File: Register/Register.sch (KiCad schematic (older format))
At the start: 22 parts, among them J1 Conn_01x16, J2 Conn_01x16, J3 Conn_01x08, J4 Conn_01x08, J5 Conn_01x12, U1 SN74LS04N, U2 74LS173, U3 74LS173, U4 74LS245

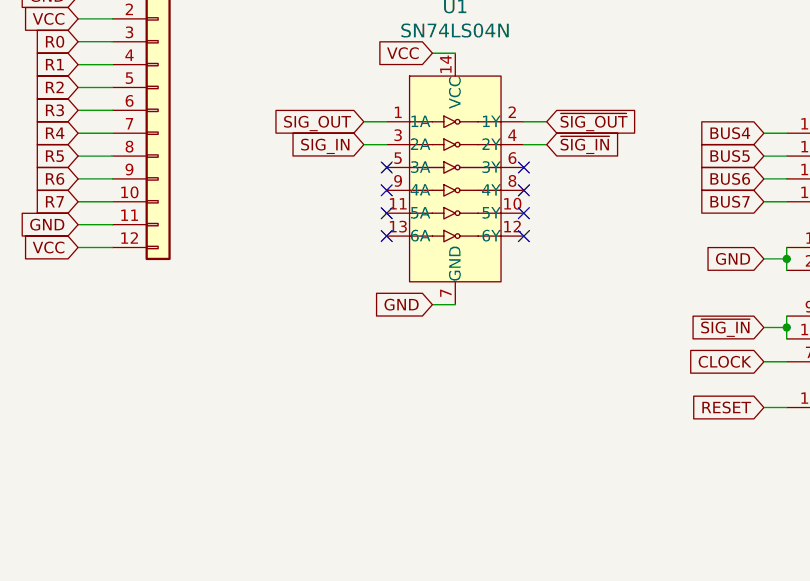
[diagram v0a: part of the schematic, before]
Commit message: Fixed floating inputs; improved power; added parts list; replaced JK latches
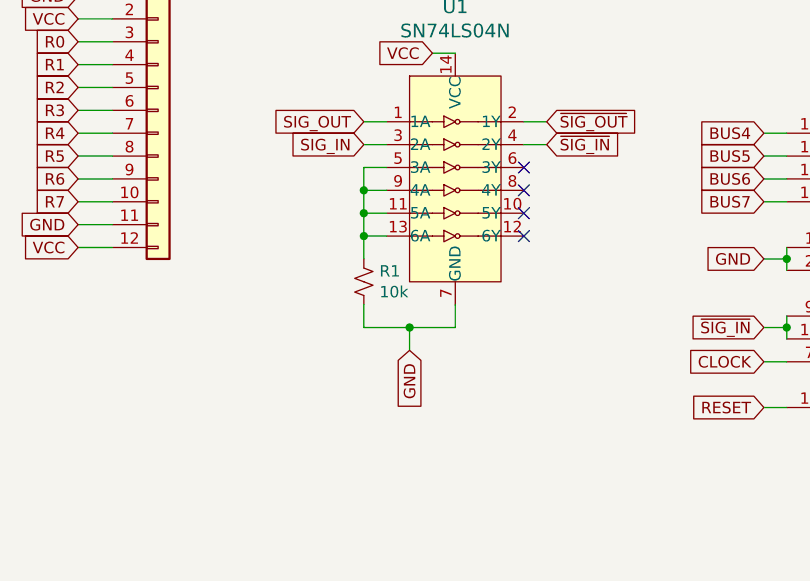
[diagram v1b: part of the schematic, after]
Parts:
- added R1: 10k, Resistor_THT:R_Axial_DIN0207_L6.3mm_D2.5mm_P7.62mm_Horizontal, symbol Device:R_Small_US
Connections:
- net GND: now also R1.1
- net at U1.11 (5A): now also U1.13 (6A), U1.5 (3A), U1.9 (4A), R1.2
- no-connect marks 8 -> 4
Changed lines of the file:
@@
 Wire Wire Line
 	8800 1750 8650 1750
-Text GLabel 4600 4100 0    50   Input ~ 0
-GND
-Wire Wire Line
-	4600 4100 4700 4100
+Text GLabel 4500 4300 3    50   Input ~ 0
+GND
 $Comp
 L Connector_Generic:Conn_01x08 J4
@@
 Wire Wire Line
 	9300 5200 9950 5200
-NoConn ~ 4400 3500
-NoConn ~ 4400 3600
-NoConn ~ 4400 3700
-NoConn ~ 4400 3800
 NoConn ~ 5000 3500
 NoConn ~ 5000 3600
@@
 Wire Wire Line
 	3050 3850 3200 3850
+Wire Wire Line
+	4400 3500 4300 3500
+Wire Wire Line
+	4300 3500 4300 3600
+Wire Wire Line
+	4400 3600 4300 3600
+Connection ~ 4300 3600
+Wire Wire Line
+	4300 3600 4300 3700
+Wire Wire Line
+	4400 3700 4300 3700
+Connection ~ 4300 3700
+Wire Wire Line
+	4300 3700 4300 3800
+Wire Wire Line
+	4400 3800 4300 3800
+$Comp
+L Device:R_Small_US R1
+U 1 1 60473EB3
+P 4300 4000
+F 0 "R1" H 4232 3954 50  0000 R CNN
+F 1 "10k" H 4232 4045 50  0000 R CNN
+F 2 "Resistor_THT:R_Axial_DIN0207_L6.3mm_D2.5mm_P7.62mm_Horizontal" H 4300 4000 50  0001 C CNN
+F 3 "~" H 4300 4000 50  0001 C CNN
+	1    4300 4000
+	-1   0    0    1
+$EndComp
+Wire Wire Line
+	4300 3800 4300 3900
+Connection ~ 4300 3800
+Wire Wire Line
+	4300 4100 4300 4200
+Wire Wire Line
+	4300 4200 4500 4200
+Wire Wire Line
+	4700 4200 4700 4100
+Wire Wire Line
+	4500 4300 4500 4200
+Connection ~ 4500 4200
+Wire Wire Line
+	4500 4200 4700 4200
 $EndSCHEMATC

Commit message: Update all boards to r3, and update revision log and gitignore
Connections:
- net R0: now also D8.2 (A); no longer D1.2 (A)
- net R1: now also D7.2 (A); no longer D2.2 (A)
- net R2: now also D6.2 (A); no longer D3.2 (A)
- net R3: now also D5.2 (A); no longer D4.2 (A)
- net R4: now also D4.2 (A); no longer D5.2 (A)
- net R5: now also D3.2 (A); no longer D6.2 (A)
- net R6: now also D2.2 (A); no longer D7.2 (A)
- net R7: now also D1.2 (A); no longer D8.2 (A)
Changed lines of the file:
@@
 Wire Wire Line
 	4150 900  4150 1050
+Text GLabel 10300 4500 1    50   Input ~ 0
+R0
+Text GLabel 9950 4500 1    50   Input ~ 0
+R1
+Text GLabel 9600 4500 1    50   Input ~ 0
+R2
+Text GLabel 9250 4500 1    50   Input ~ 0
+R3
+Text GLabel 8850 4500 1    50   Input ~ 0
+R4
+Text GLabel 8500 4500 1    50   Input ~ 0
+R5
+Text GLabel 8150 4500 1    50   Input ~ 0
+R6
 Text GLabel 7800 4500 1    50   Input ~ 0
-R0
-Text GLabel 8150 4500 1    50   Input ~ 0
-R1
-Text GLabel 8500 4500 1    50   Input ~ 0
-R2
-Text GLabel 8850 4500 1    50   Input ~ 0
-R3
-Text GLabel 9250 4500 1    50   Input ~ 0
-R4
-Text GLabel 9600 4500 1    50   Input ~ 0
-R5
-Text GLabel 9950 4500 1    50   Input ~ 0
-R6
-Text GLabel 10300 4500 1    50   Input ~ 0
 R7
 Wire Wire Line
